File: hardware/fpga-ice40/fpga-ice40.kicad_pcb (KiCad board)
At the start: 4 copper layers, 53.4 x 49.2 mm, 99 parts, among them J1 Conn_01x03, J2 MicroSD_Molex_1040310811, J3 FTSH-105-01-L-DV-K, J4 FTSH-105-01-L-DV-K, J5 USB_B_Micro, J6 Conn_02x20_Odd_Even, Q1 2N7002H-7, U1 iCE40HX4K-TQ144, U10 MC74HC1G08DTT1G, U11 USBLC6-2SC6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

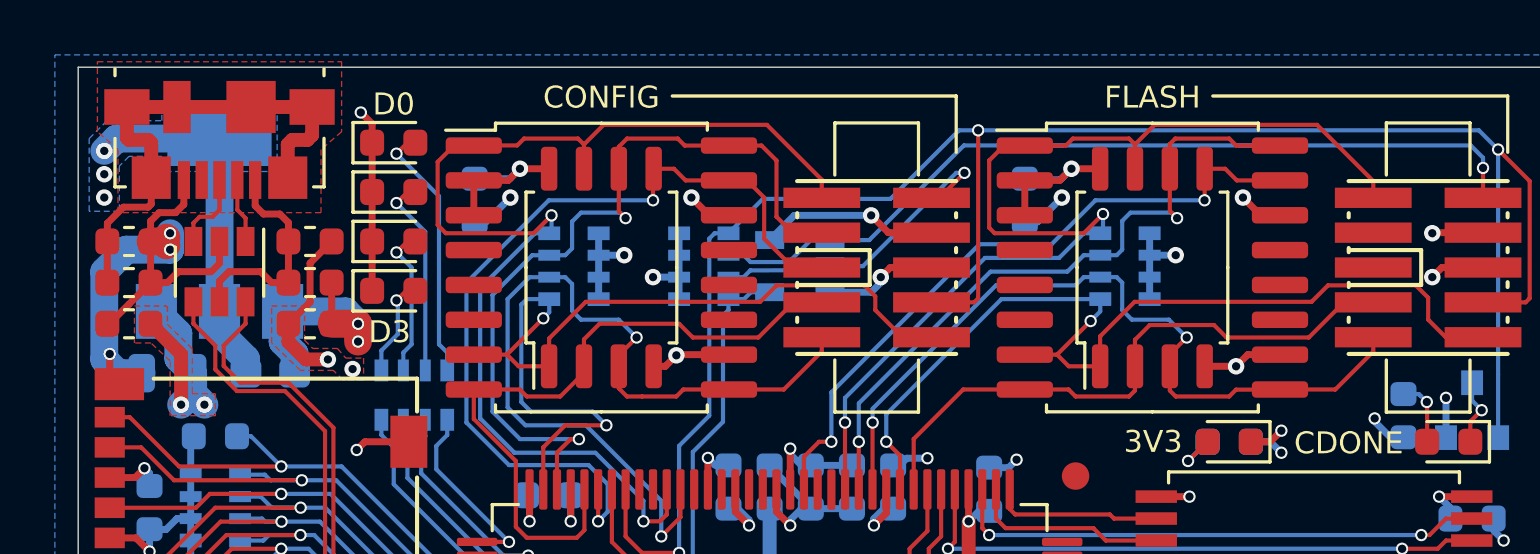
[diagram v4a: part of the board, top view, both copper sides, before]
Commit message: Fix DRC violations and unconnected nets
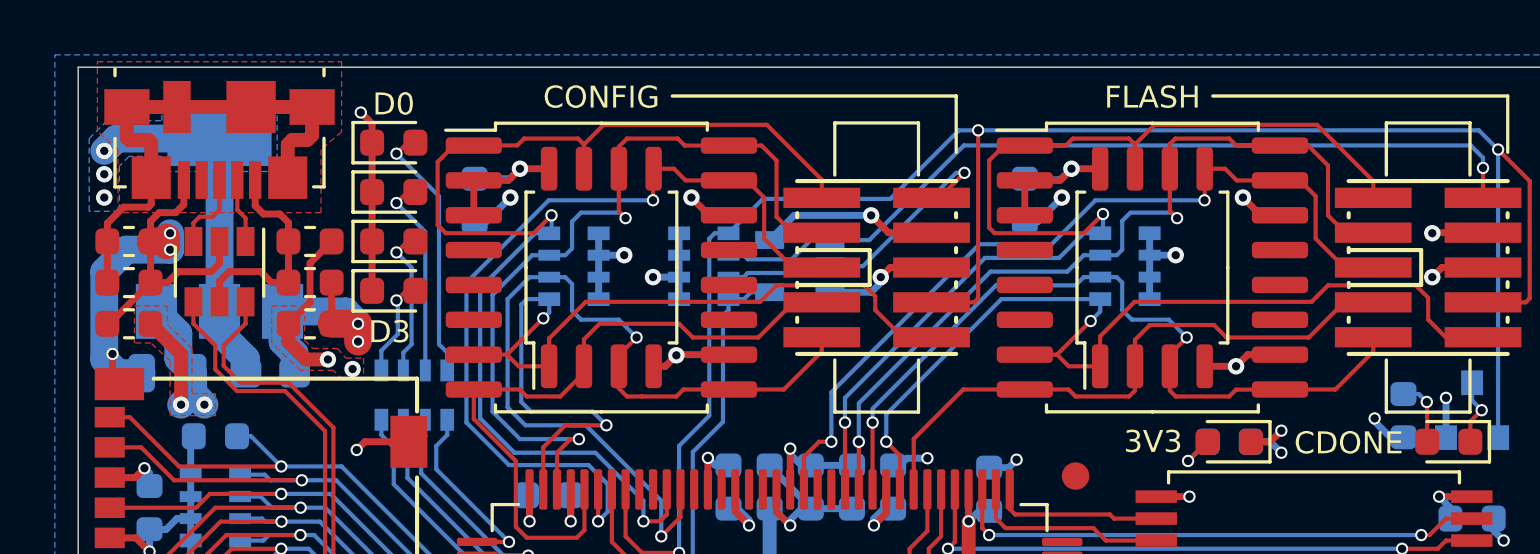
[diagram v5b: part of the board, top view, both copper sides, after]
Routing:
- net FLASH_SCK: track 25.3 -> 31.1 mm
- net FLASH_MOSI|IO0: track 24.8 -> 30.4 mm
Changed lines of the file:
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@@
     (thickness 1.2)
     (drawings 23)
-    (tracks 1802)
+    (tracks 1812)
     (zones 0)
     (modules 99)
@@
   (layers
     (0 F.Cu signal)
-    (1 "In1(GND).Cu" power hide)
-    (2 "In2(PWR).Cu" power hide)
+    (1 "In1(GND).Cu" power)
+    (2 "In2(PWR).Cu" power)
     (31 B.Cu signal)
     (32 B.Adhes user hide)
@@
   (segment (start 141.6875 90.7625) (end 142.05 90.4) (width 0.254) (layer B.Cu) (net 12))
   (segment (start 141.6875 91.65) (end 141.6875 90.7625) (width 0.254) (layer B.Cu) (net 12))
-  (via (at 137.000002 79.4) (size 0.45) (drill 0.3) (layers F.Cu B.Cu) (net 12))
-  (segment (start 137 79.400002) (end 137.000002 79.4) (width 0.254) (layer F.Cu) (net 12))
   (segment (start 169.6625 110.7375) (end 169.6625 109.6) (width 0.508) (layer F.Cu) (net 12))
   (segment (start 168.85 111.55) (end 169.6625 110.7375) (width 0.508) (layer F.Cu) (net 12))
@@
   (segment (start 153.8 84.3375) (end 153.8 85.499998) (width 0.254) (layer F.Cu) (net 12))
   (segment (start 163.25 77.15) (end 163.05 77.15) (width 0.254) (layer B.Cu) (net 12))
-  (segment (start 137.000002 80.150002) (end 137.35 80.5) (width 0.254) (layer F.Cu) (net 12))
-  (segment (start 137.000002 79.4) (end 137.000002 80.150002) (width 0.254) (layer F.Cu) (net 12))
   (segment (start 152.47 116.95) (end 164.99 116.95) (width 0.254) (layer F.Cu) (net 12))
   (segment (start 164.99 116.95) (end 166.35 115.59) (width 0.254) (layer F.Cu) (net 12))
@@
   (segment (start 145.4125 104.3) (end 144.9 104.3) (width 0.254) (layer B.Cu) (net 12))
   (segment (start 144.9 104.3) (end 144.45 104.75) (width 0.254) (layer B.Cu) (net 12))
+  (via (at 137.1 79.4) (size 0.45) (drill 0.3) (layers F.Cu B.Cu) (net 12))
+  (segment (start 137 79.400002) (end 137.000002 79.4) (width 0.254) (layer F.Cu) (net 12))
+  (segment (start 137.000002 79.4) (end 137.1 79.4) (width 0.254) (layer F.Cu) (net 12))
+  (segment (start 137.35 80.5) (end 137.1 80.25) (width 0.254) (layer F.Cu) (net 12))
+  (segment (start 137.1 80.25) (end 137.1 79.4) (width 0.254) (layer F.Cu) (net 12))
   (segment (start 158.85 81.65) (end 157.75 82.75) (width 0.1524) (layer B.Cu) (net 19))
   (segment (start 157.75 82.75) (end 157.75 86.649998) (width 0.1524) (layer B.Cu) (net 19))
@@
   (segment (start 145.3625 96.05) (end 145.4125 96) (width 0.1524) (layer B.Cu) (net 137))
   (segment (start 144.6 96.05) (end 145.3625 96.05) (width 0.1524) (layer B.Cu) (net 137))
-  (segment (start 162.395189 76.354811) (end 162.55 76.2) (width 0.1524) (layer B.Cu) (net 150))
-  (segment (start 160.098 76.602) (end 160.345189 76.354811) (width 0.1524) (layer B.Cu) (net 150))
-  (segment (start 162.55 76.2) (end 163.25 76.2) (width 0.1524) (layer B.Cu) (net 150))
-  (segment (start 159.55 76.602) (end 160.098 76.602) (width 0.1524) (layer B.Cu) (net 150))
-  (segment (start 162.2 76.35) (end 162.395189 76.354811) (width 0.1524) (layer B.Cu) (net 150))
-  (segment (start 160.345189 76.354811) (end 162.2 76.35) (width 0.1524) (layer B.Cu) (net 150))
-  (segment (start 161.75 76.05) (end 162.55 75.25) (width 0.1524) (layer B.Cu) (net 151))
-  (segment (start 160.102 75.802) (end 160.35 76.05) (width 0.1524) (layer B.Cu) (net 151))
-  (segment (start 162.55 75.25) (end 163.25 75.25) (width 0.1524) (layer B.Cu) (net 151))
-  (segment (start 160.35 76.05) (end 161.75 76.05) (width 0.1524) (layer B.Cu) (net 151))
-  (segment (start 159.55 75.802) (end 160.102 75.802) (width 0.1524) (layer B.Cu) (net 151))
   (segment (start 183.05 79.3124) (end 183.05 78.79) (width 0.1524) (layer F.Cu) (net 26))
   (segment (start 181.6674 80.695) (end 183.05 79.3124) (width 0.1524) (layer F.Cu) (net 26))
   (segment (start 179.65 80.695) (end 181.6674 80.695) (width 0.1524) (layer F.Cu) (net 26))
+  (segment (start 182 76.25) (end 183.05 76.25) (width 0.1524) (layer F.Cu) (net 28))
+  (segment (start 180.95 75.2) (end 182 76.25) (width 0.1524) (layer F.Cu) (net 28))
+  (segment (start 180.95 73.65) (end 180.95 75.2) (width 0.1524) (layer F.Cu) (net 28))
+  (segment (start 180.375 73.075) (end 180.95 73.65) (width 0.1524) (layer F.Cu) (net 28))
+  (segment (start 179.65 73.075) (end 180.375 73.075) (width 0.1524) (layer F.Cu) (net 28))
+  (segment (start 182.03 74.98) (end 183.05 74.98) (width 0.1524) (layer F.Cu) (net 29))
+  (segment (start 181.4 74.35) (end 182.03 74.98) (width 0.1524) (layer F.Cu) (net 29))
+  (segment (start 181.4 72.53) (end 181.4 74.35) (width 0.1524) (layer F.Cu) (net 29))
+  (segment (start 180.675 71.805) (end 181.4 72.53) (width 0.1524) (layer F.Cu) (net 29))
+  (segment (start 179.65 71.805) (end 180.675 71.805) (width 0.1524) (layer F.Cu) (net 29))
   (segment (start 162.95 79.3124) (end 162.95 78.79) (width 0.1524) (layer F.Cu) (net 31))
   (segment (start 161.5674 80.695) (end 162.95 79.3124) (width 0.1524) (layer F.Cu) (net 31))
@@
   (segment (start 167.85 72.8) (end 168.15 72.8) (width 0.1524) (layer B.Cu) (net 150))
   (segment (start 163.25 76.2) (end 164.45 76.2) (width 0.1524) (layer B.Cu) (net 150))
+  (segment (start 162.3 76.45) (end 162.55 76.2) (width 0.1524) (layer B.Cu) (net 150))
+  (segment (start 160.25 76.45) (end 162.3 76.45) (width 0.1524) (layer B.Cu) (net 150))
+  (segment (start 160.098 76.602) (end 160.25 76.45) (width 0.1524) (layer B.Cu) (net 150))
+  (segment (start 162.55 76.2) (end 163.25 76.2) (width 0.1524) (layer B.Cu) (net 150))
+  (segment (start 159.55 76.602) (end 160.098 76.602) (width 0.1524) (layer B.Cu) (net 150))
   (via (at 187.05 72.620751) (size 0.45) (drill 0.3) (layers F.Cu B.Cu) (net 151))
   (segment (start 187.05 73.71) (end 187.05 72.620751) (width 0.1524) (layer F.Cu) (net 151))
@@
   (segment (start 186.6 71.8) (end 187.05 72.25) (width 0.1524) (layer B.Cu) (net 151))
   (segment (start 163.25 75.25) (end 164.681064 75.25) (width 0.1524) (layer B.Cu) (net 151))
+  (segment (start 162.55 75.25) (end 163.25 75.25) (width 0.1524) (layer B.Cu) (net 151))
+  (segment (start 161.85 75.95) (end 162.55 75.25) (width 0.1524) (layer B.Cu) (net 151))
+  (segment (start 160.25 75.95) (end 161.85 75.95) (width 0.1524) (layer B.Cu) (net 151))
+  (segment (start 160.102 75.802) (end 160.25 75.95) (width 0.1524) (layer B.Cu) (net 151))
+  (segment (start 159.55 75.802) (end 160.102 75.802) (width 0.1524) (layer B.Cu) (net 151))
   (via (at 151.55 91.75) (size 0.45) (drill 0.3) (layers F.Cu B.Cu) (net 152))
   (via (at 143.25 86.5) (size 0.45) (drill 0.3) (layers F.Cu B.Cu) (net 152))

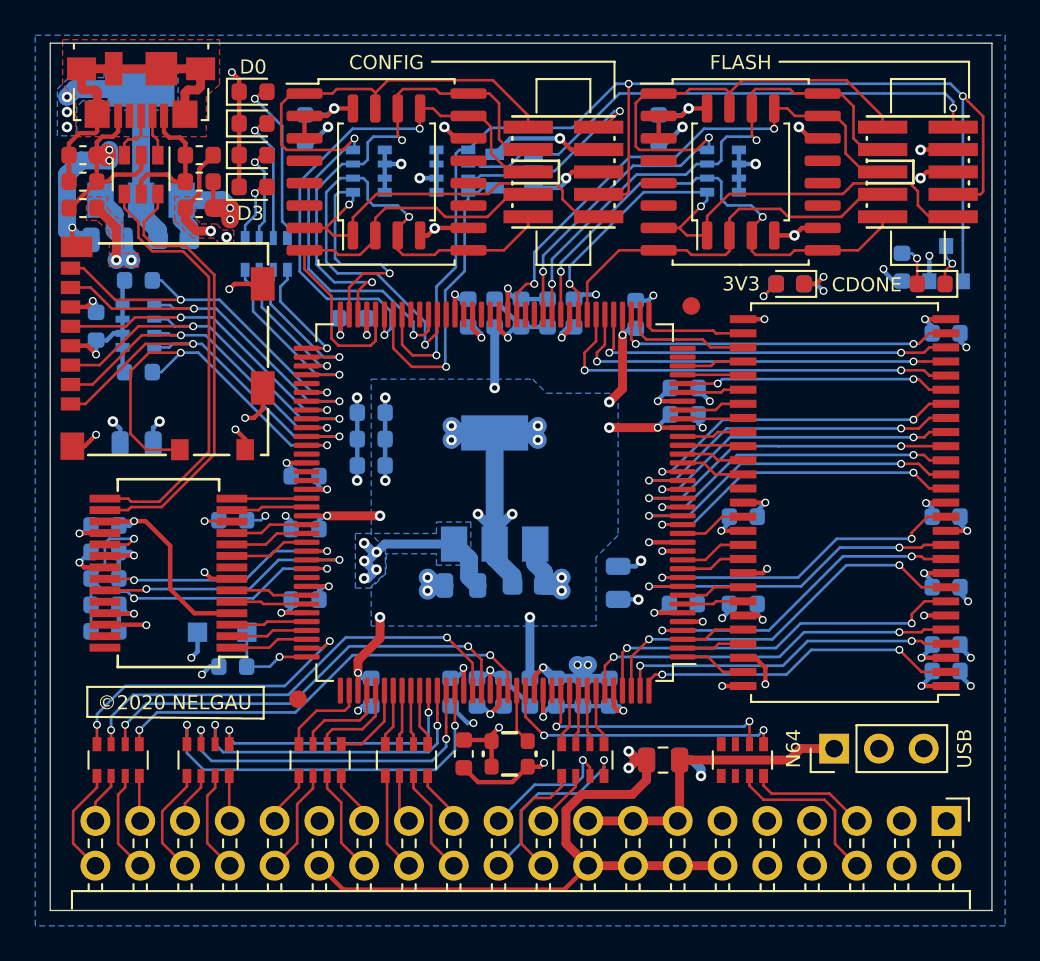
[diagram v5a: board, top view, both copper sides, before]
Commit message: Confirmed controlled impedance and decoupling specifications
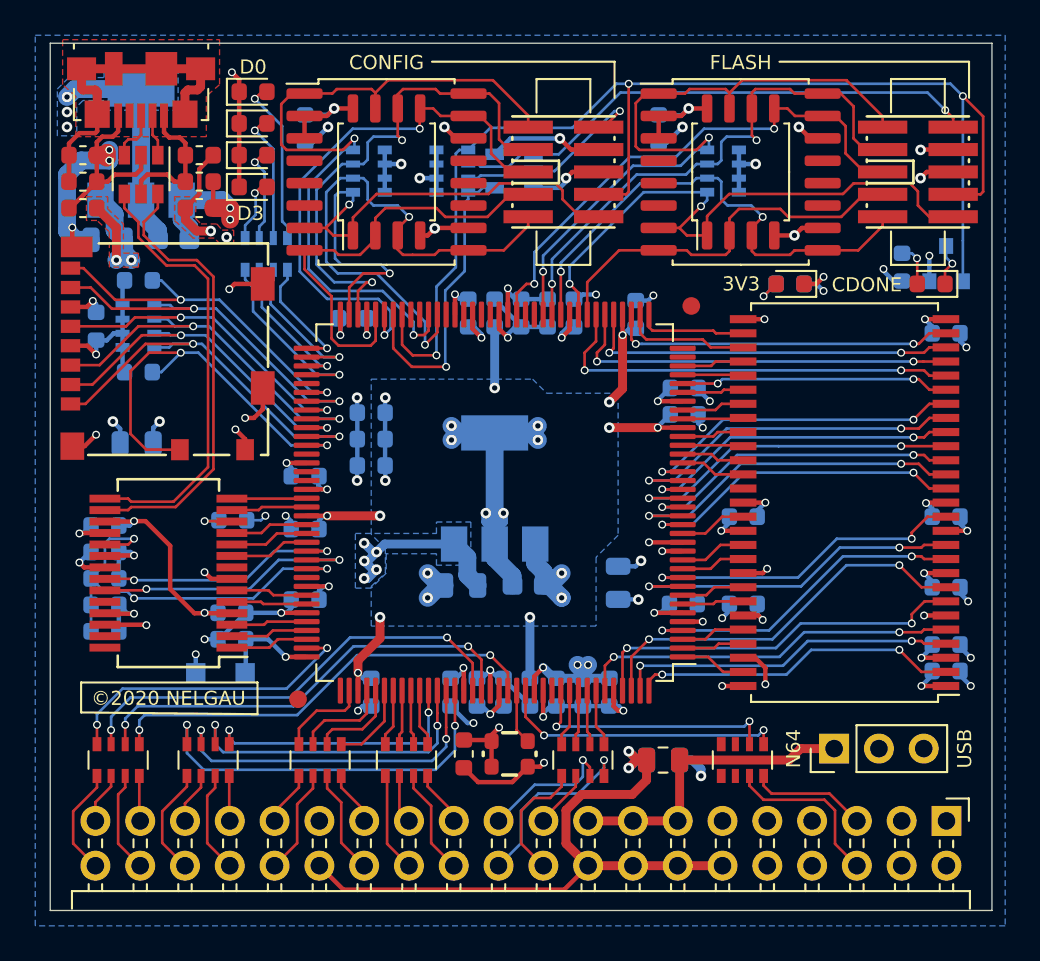
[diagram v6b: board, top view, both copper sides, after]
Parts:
- added C50: 100n, Capacitor_SMD:C_0603_1608Metric, B.Cu at (146.2, 101.2)
- moved D1 2.30 mm to (145.5, 104.7)
- moved C29 1.55 mm to (146.2, 102.8)
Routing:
- net GND: track 182.8 -> 187.2 mm
- net /Interface_USB/USB_VIO: track 11.8 -> 12.5 mm, vias 1 -> 2
- net N64_AD15: track 18.1 -> 17.5 mm
- net P3V3: track 109.8 -> 109.3 mm
- net FLASH_CRESETn: track 30.9 -> 30.4 mm
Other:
- net class DRAM added: clearance 0.1524, trace_width 0.1524, via_dia 0.45, via_drill 0.3
